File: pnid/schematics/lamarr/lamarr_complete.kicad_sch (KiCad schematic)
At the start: 72 parts

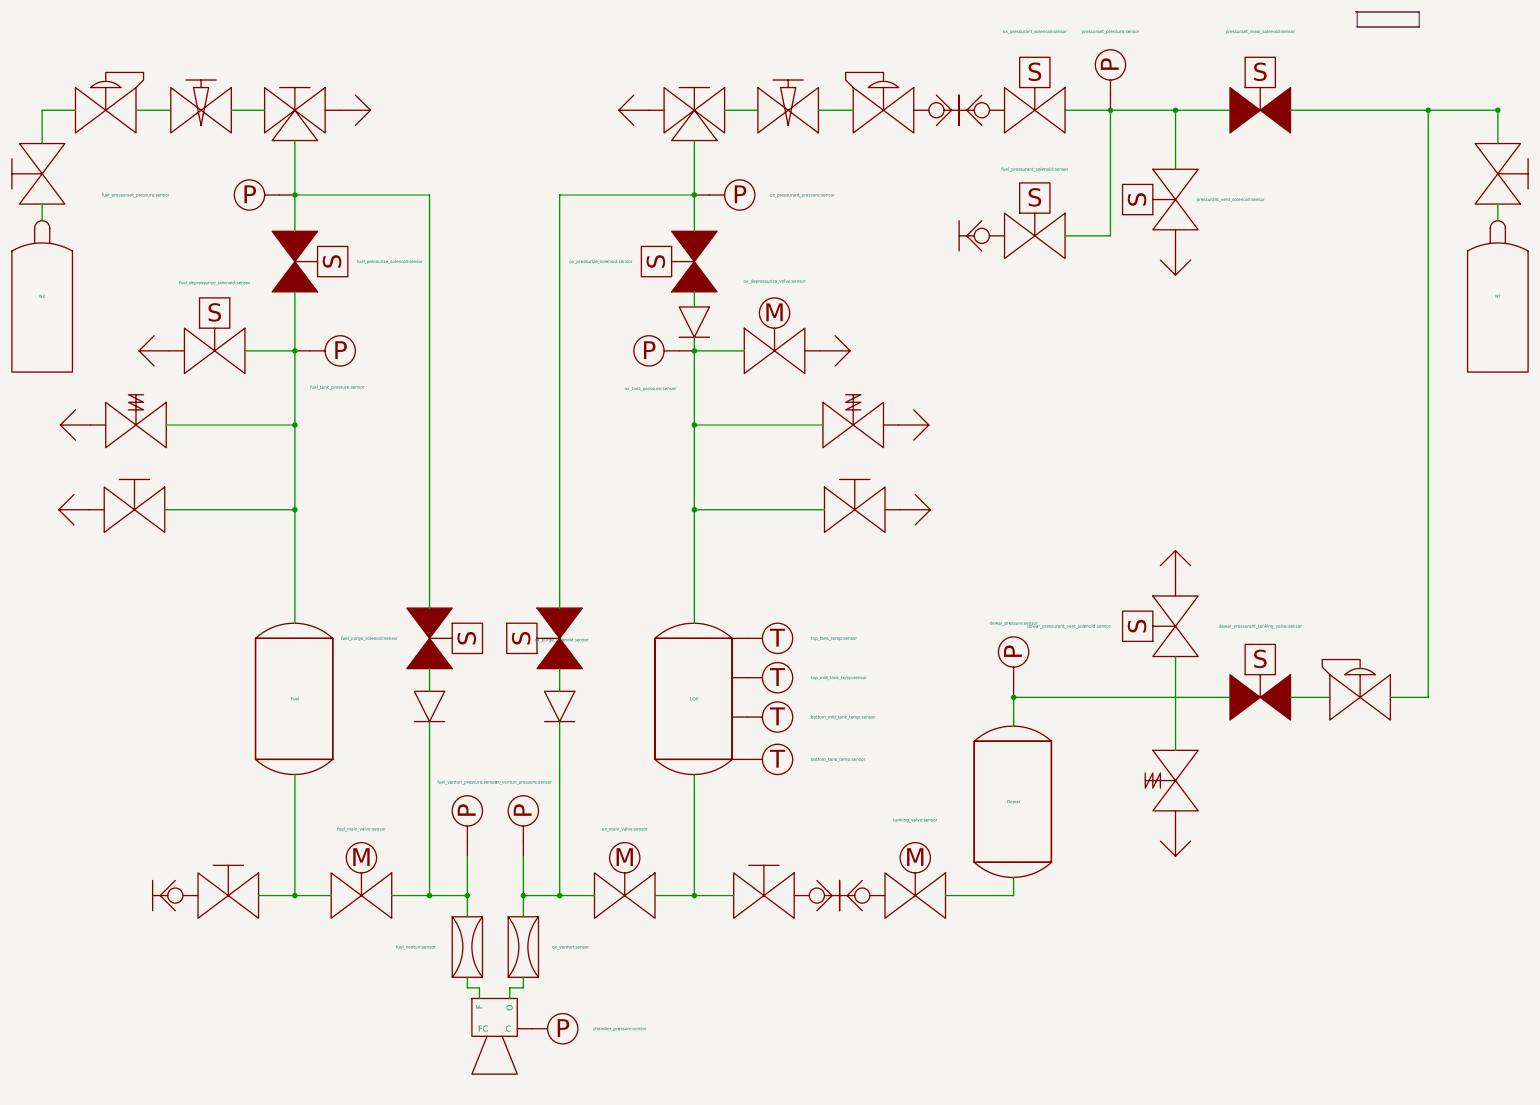
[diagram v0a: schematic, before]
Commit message: update schematics to kicad 8
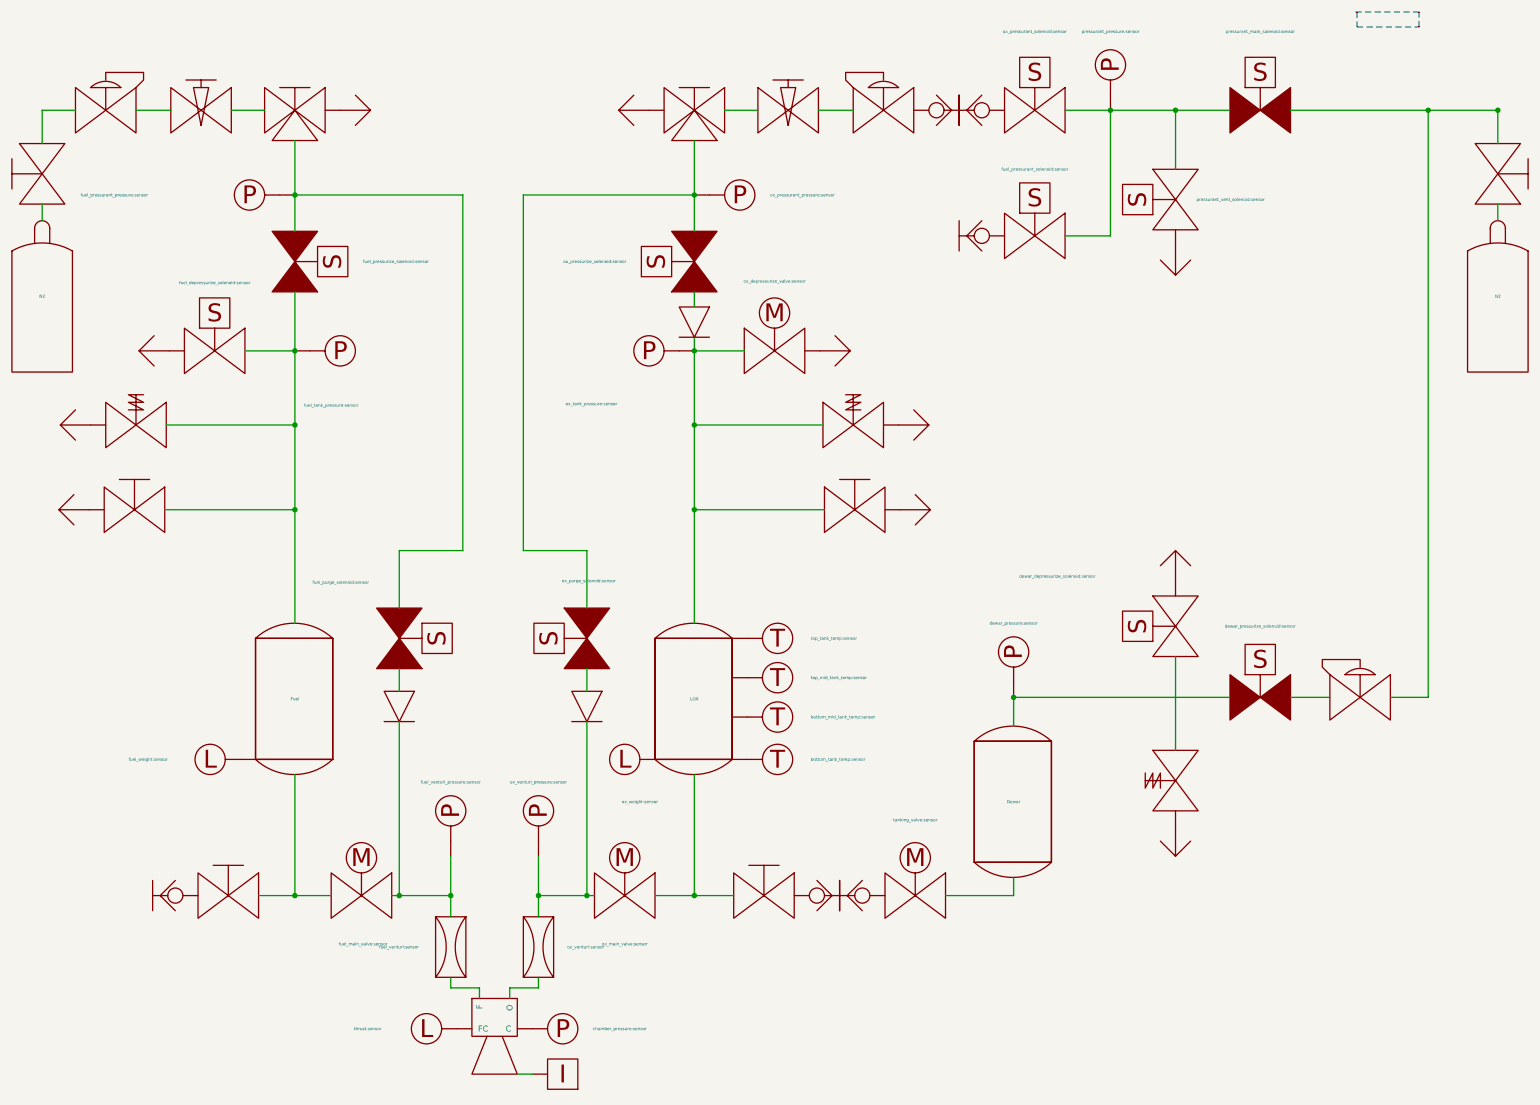
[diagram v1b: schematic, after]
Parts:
- removed Vent?: Vent, symbol PnID-Lib:Vent
- added Vent?: Vent, symbol lamarr_complete-rescue:Vent-PnID-Lib
- added fuel_weight: fuel_weight:sensor, symbol lamarr_complete-rescue:Sensor_Load-PnID-Lib
- added igniter: igniter:sensor, symbol lamarr_complete-rescue:igniter-PnID-Lib
- added ox_weight: ox_weight:sensor, symbol lamarr_complete-rescue:Sensor_Load_Short-PnID-Lib
- added thrust: thrust:sensor, symbol lamarr_complete-rescue:Sensor_Load-PnID-Lib
- CheckValve? (x3): symbol PnID-Lib:CheckValve -> lamarr_complete-rescue:CheckValve-PnID-Lib
- Dewar, Fuel, LOX: symbol PnID-Lib:Tank_Slim -> lamarr_complete-rescue:Tank_Slim-PnID-Lib
- DewarOverPressureValve?, fuel_safety_valve, ox_safety_valve: symbol PnID-Lib:Valve_OverPressure -> lamarr_complete-rescue:Valve_OverPressure-PnID-Lib
- DewarPressureRegulator?, fuel_pressure_regulator, ox_pressure_regulator: symbol PnID-Lib:PressureRegulator -> lamarr_complete-rescue:PressureRegulator-PnID-Lib
- DewarQuickConnect?, QuickConnect?, fuel_quick_connect, fuel_quick_connect?, ox_quick_connect, ox_quick_connect?: symbol PnID-Lib:QuickConnect_Half -> lamarr_complete-rescue:QuickConnect_Half-PnID-Lib
- N2: symbol PnID-Lib:GasBottle -> lamarr_complete-rescue:GasBottle-PnID-Lib
- N2: renamed from N?; symbol PnID-Lib:GasBottle -> lamarr_complete-rescue:GasBottle-PnID-Lib
- Vent? (x10): symbol PnID-Lib:Vent -> lamarr_complete-rescue:Vent-PnID-Lib
- bottom_mid_tank_temp, bottom_tank_temp, top_mid_tank_temp, top_tank_temp: symbol PnID-Lib:Sensor_Temperature -> lamarr_complete-rescue:Sensor_Temperature-PnID-Lib
- chamber_pressure, dewar_pressure?, fuel_pressurant_pressure, fuel_tank_pressure, fuel_venturi_pressure, ox_pressurant_pressure:sensor, ox_tank_pressure, ox_venturi_pressure, pressurant_pressure?: symbol PnID-Lib:Sensor_Pressure -> lamarr_complete-rescue:Sensor_Pressure-PnID-Lib
- dewar_depressurize_solenoid?: renamed from dewar_pressurant_vent_solenoid?; value dewar_pressurant_vent_solenoid:sensor -> dewar_depressurize_solenoid:sensor; symbol PnID-Lib:Valve_Solenoid_NO -> lamarr_complete-rescue:Valve_Solenoid_NO-PnID-Lib
- dewar_pressurize_solenoid?: renamed from dewar_pressurant_tanking_valve?; value dewar_pressurant_tanking_valve:sensor -> dewar_pressurize_solenoid:sensor; symbol PnID-Lib:Valve_Solenoid_NC -> lamarr_complete-rescue:Valve_Solenoid_NC-PnID-Lib
- engine: symbol PnID-Lib:Engine -> lamarr_complete-rescue:Engine-PnID-Lib
- fuel_depressurize_solenoid, fuel_pressurant_solenoid?, ox_pressurant_solenoid?, pressurant_vent_solenoid?: symbol PnID-Lib:Valve_Solenoid_NO -> lamarr_complete-rescue:Valve_Solenoid_NO-PnID-Lib
- fuel_main_valve, ox_depressurize_valve, ox_main_valve, tanking_valve?: symbol PnID-Lib:Valve_Servo -> lamarr_complete-rescue:Valve_Servo-PnID-Lib
- fuel_manual_3way, fuel_manual_3way?: symbol PnID-Lib:Valve_Manual_3Way -> lamarr_complete-rescue:Valve_Manual_3Way-PnID-Lib
- fuel_manual_tanking_valve, fuel_manual_valve, fuel_manual_vent_valve, ox_manual_tanking_valve, ox_manual_valve, ox_manual_vent_valve: symbol PnID-Lib:Valve_Manual -> lamarr_complete-rescue:Valve_Manual-PnID-Lib
- fuel_needle_valve, ox_needle_valve: symbol PnID-Lib:Valve_Needle -> lamarr_complete-rescue:Valve_Needle-PnID-Lib
- fuel_pressurize_solenoid, fuel_purge_solenoid, ox_pressurize_solenoid, ox_purge_solenoid, pressurant_main_solenoid?: symbol PnID-Lib:Valve_Solenoid_NC -> lamarr_complete-rescue:Valve_Solenoid_NC-PnID-Lib
- fuel_venturi, ox_venturi: symbol PnID-Lib:Venturi -> lamarr_complete-rescue:Venturi-PnID-Lib
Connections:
- net at engine.~ (O): now also thrust.~
- net at ox_venturi.~: now also CheckValve?.~, ox_main_valve.~, ox_venturi_pressure.~; no longer engine.~ (O)
- net at fuel_venturi.~: now also CheckValve?.~, fuel_main_valve.~, fuel_venturi_pressure.~; no longer engine.~ (O)
- net at DewarPressureRegulator?.~: now also ox_manual_valve.~, pressurant_main_solenoid?.~; no longer dewar_pressurize_solenoid?.~
- net at DewarOverPressureValve?.~: now also Vent?.~; no longer dewar_depressurize_solenoid?.~
- net at ox_manual_vent_valve.~: now also Vent?.~
- new net: fuel_manual_3way?.~, ox_pressurant_pressure:sensor.~, ox_pressurize_solenoid.~, ox_purge_solenoid.~
- new net: fuel_manual_3way.~, fuel_pressurant_pressure.~, fuel_pressurize_solenoid.~, fuel_purge_solenoid.~
- new net: Fuel.~, fuel_depressurize_solenoid.~, fuel_manual_vent_valve.~, fuel_pressurize_solenoid.~, fuel_safety_valve.~, fuel_tank_pressure.~
- new net: CheckValve?.~, LOX.~, ox_depressurize_valve.~, ox_manual_vent_valve.~, ox_safety_valve.~, ox_tank_pressure.~
- new net: LOX.~, ox_main_valve.~, ox_manual_tanking_valve.~
- new net: Fuel.~, fuel_main_valve.~, fuel_manual_tanking_valve.~
- new net: engine.~ (O), ox_venturi.~
- new net: engine.~ (O), fuel_venturi.~
- new net: DewarPressureRegulator?.~, dewar_pressurize_solenoid?.~
- new net: DewarOverPressureValve?.~, dewar_depressurize_solenoid?.~
- new net: fuel_pressurant_solenoid?.~, ox_pressurant_solenoid?.~, pressurant_main_solenoid?.~, pressurant_pressure?.~, pressurant_vent_solenoid?.~
